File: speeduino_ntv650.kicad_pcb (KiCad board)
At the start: 2 copper layers, 105.1 x 96.7 mm, 70 parts, among them IC1 SP721, IC2 TC4424, J1 Conn_01x25_DB-25, P1 MAX9926_9927, Q1 STP62NS04Z, Q2 STP62NS04Z, Q3 STP62NS04Z, U1 LM2937xT

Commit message: first complited pcb
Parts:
- moved C13 52.2 mm to (108.2, 55.2)
- moved R9 37.3 mm to (91.2, 42.7), turned to 90 degrees
- moved C4 34.0 mm to (120.6, 55.2)
- moved C10 28.3 mm to (152.7, 81.3), turned to 0 degrees
- moved R18 26.0 mm to (108.8, 98.3), turned to 90 degrees
- moved C6 25.5 mm to (120.7, 40.9), turned to 270 degrees
- moved R14 23.8 mm to (105.8, 72.1)
- moved C8 23.4 mm to (132.2, 55.2), turned to 270 degrees
- moved C15 22.3 mm to (152.9, 89.1), turned to 0 degrees
- moved C16 20.9 mm to (126.7, 55.2), turned to 270 degrees
- moved R31 16.0 mm to (103.1, 98.4)
- moved R10 14.6 mm to (108.3, 45.9)
- moved R15 14.6 mm to (113.1, 45.9)
- moved R29 14.6 mm to (103.6, 45.9)
- moved R30 14.6 mm to (98.8, 45.9)
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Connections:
- C5 pad 1: MAP_5V -> 5V
- C6 pad 1: MAP_5V -> 5V
- J1 pad 16: MAP_5V -> 5V
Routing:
- net GND: track 485.5 -> 62.9 mm, vias 0 -> 12
- net 5V: track 240.8 -> 412.2 mm, vias 4 -> 2
- net MAP_5V: track 68.1 -> 0.00 mm, vias 2 -> 0
- net ADC-Clamp3: track 83.5 -> 138.1 mm
- net ADC-Clamp4: track 141.6 -> 93.0 mm
- net Net-(C2-Pad1): track 6.65 -> 49.4 mm
- net TACH2-CPU-D18: track 22.9 -> 60.9 mm, vias 0 -> 1
- net ADC-Clamp2: track 84.3 -> 121.2 mm, vias 2 -> 3
- net TPS_sens: track 176.4 -> 142.2 mm, vias 2 -> 1
- net Net-(C2-Pad2): track 5.64 -> 36.6 mm
- net ADC-Clamp1: track 103.5 -> 73.4 mm, vias 4 -> 1
- net ADC-Clamp6: track 102.3 -> 72.7 mm
- net Net-(C13-Pad1): track 103.4 -> 73.9 mm, vias 3 -> 0
- net IDLE-CPU-D6: track 70.5 -> 41.2 mm, vias 2 -> 0
- net MAP-CPU-A3: track 102.6 -> 74.2 mm, vias 1 -> 4
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- added copper zone on F.Cu, net (none)
- added copper zone on B.Cu, net GND
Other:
- board size 105.1 x 96.7 mm -> 105.2 x 102 mm
- net class 5v_small: clearance 0.11 -> 0.2; via_dia 0.8 -> 1.2; via_drill 0.4 -> 0.2
- net class Default: clearance 0.4 -> 0.2; via_dia 0.8 -> 1.2; via_drill 0.4 -> 0.2
- net class GND_MOSFIT: clearance 0.4 -> 0.3; via_dia 1 -> 1.2; via_drill 0.8 -> 0.2
- net class POWER_ENG: clearance 0.4 -> 0.28; via_dia 0.8 -> 1.2; via_drill 0.4 -> 0.2
- net class Power: clearance 0.4 -> 0.22; via_dia 1 -> 1.2; via_drill 0.6 -> 0.2
- net class power_exit: clearance 0.4 -> 0.3; via_dia 0.8 -> 1.2; via_drill 0.4 -> 0.2
- net class power_logic: via_dia 0.8 -> 1.2; via_drill 0.7 -> 0.2
- net class step_engine_exit: clearance 0.4 -> 0.3; via_dia 0.8 -> 1.2; via_drill 0.4 -> 0.2
- rule trace_clearance: 0.4 -> 0.2
- rule via_min_drill: 0.3 -> 0.2
- rule via_min_size: 0.4 -> 0.1

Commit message: new routes
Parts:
- C1, C11, C14, C2: moved to F.Cu
- moved R32 31.3 mm to (107.8, 107.7)
- moved R19 31.3 mm to (101.9, 107.9)
- moved R21 17.9 mm to (90.8, 89.0)
- moved R22 17.7 mm to (84.9, 89.0)
- moved R18 17.4 mm to (123.2, 108.2)
- moved R31 17.4 mm to (117.5, 108.2)
- moved C11 7.34 mm to (101.4, 62.5), turned to 90 degrees
- moved R1 3.45 mm to (137.2, 107.8)
- moved R2 3.45 mm to (131.8, 108.0)
- moved C18 3.11 mm to (74.5, 55.0)
- moved R25 0.72 mm to (121.7, 72.1)
- moved R23 0.31 mm to (114.7, 72.1)
- moved R24 0.31 mm to (135.1, 72.1)
- moved R26 0.31 mm to (128.3, 72.1)
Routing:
- net GND: track 62.9 -> 0.00 mm, vias 12 -> 0
- net 5V: track 412.2 -> 359.8 mm
- net MAP-CPU-A3: track 74.2 -> 122.7 mm, vias 4 -> 0
- net INJ2-CPU-D9: track 108.3 -> 67.8 mm, vias 1 -> 0
- net ADC-Clamp2: track 121.2 -> 85.6 mm, vias 3 -> 1
- net Net-(Q3-Pad1): track 18.3 -> 48.3 mm
- net ign-2-out: track 64.8 -> 93.8 mm, vias 1 -> 0
- net IDLE-CPU-D6: track 41.2 -> 13.3 mm
- net Net-(Q1-Pad1): track 8.40 -> 36.1 mm
- net Net-(C13-Pad1): track 73.9 -> 48.9 mm
- net INJ1-CPU-D8: track 50.1 -> 27.3 mm
- net ADC-Clamp3: track 138.1 -> 123.1 mm
- net Net-(Q2-Pad1): track 21.7 -> 7.96 mm
- net Net-(IC2-Pad7): track 21.9 -> 35.4 mm
- net ADC-Clamp4: track 93.0 -> 106.1 mm, vias 1 -> 2
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- added copper zone on F.Cu, net GND
- removed copper zone on F.Cu, net (none)

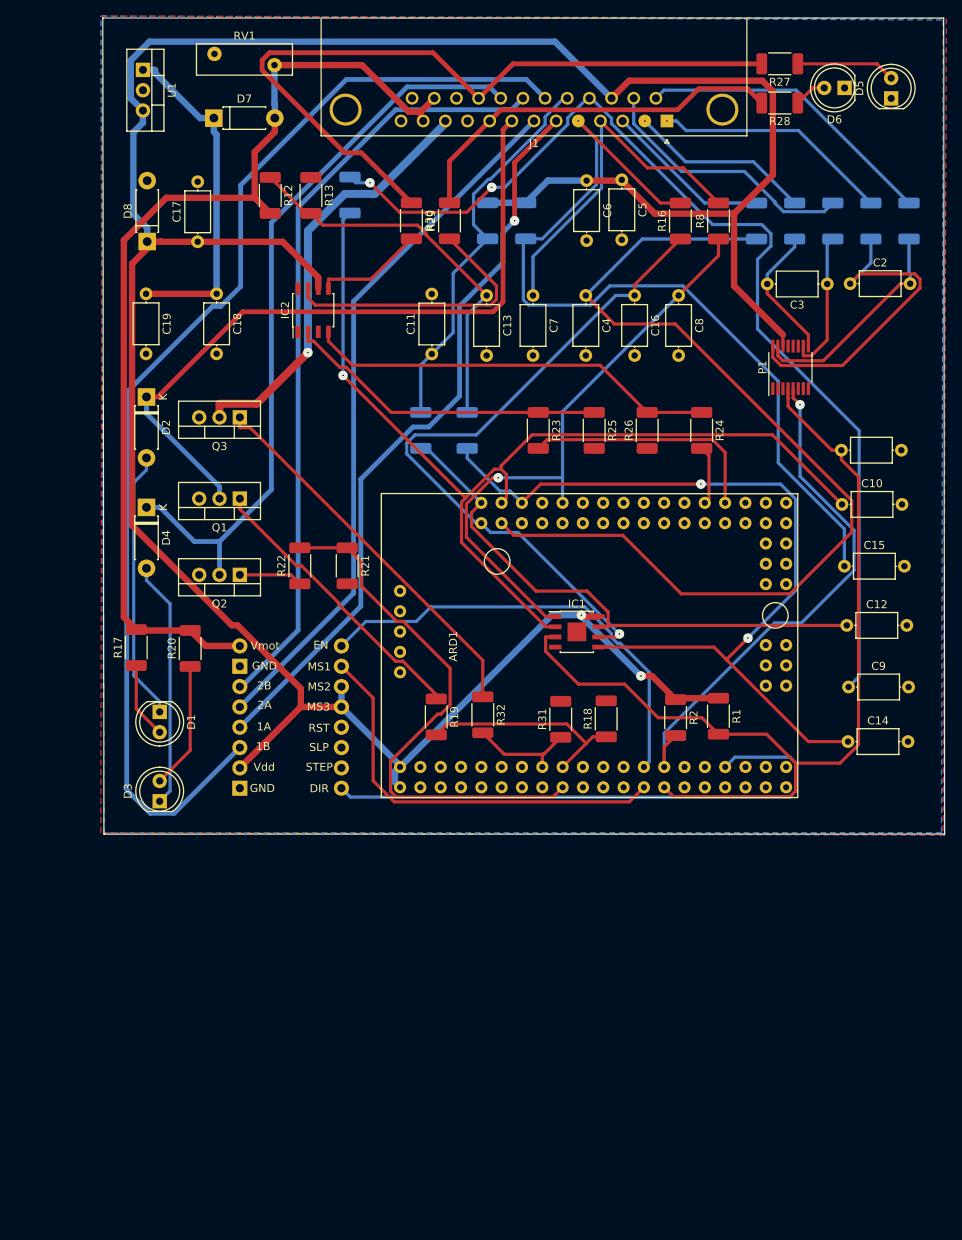
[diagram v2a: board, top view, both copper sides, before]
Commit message: pcb size chaged
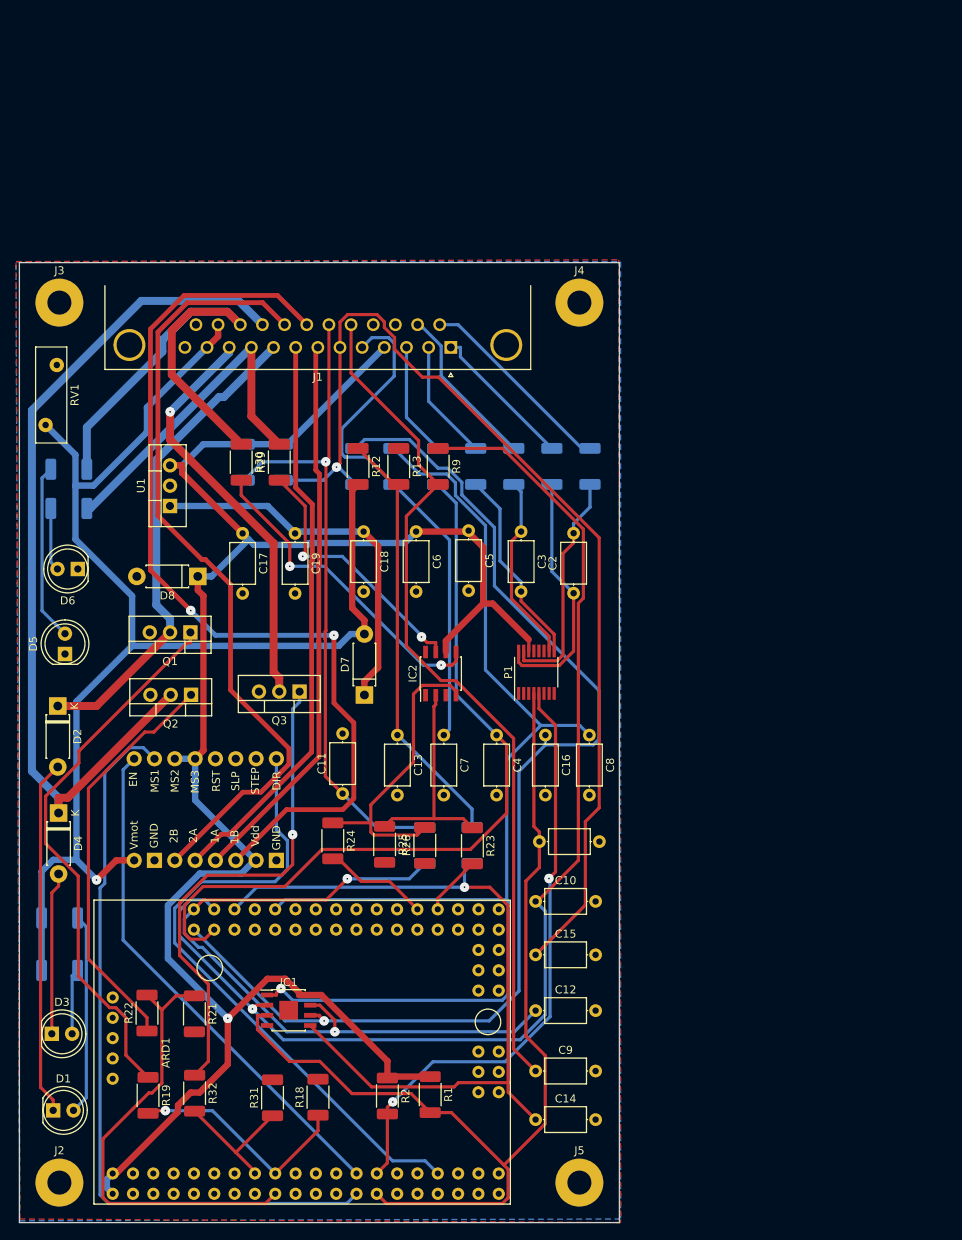
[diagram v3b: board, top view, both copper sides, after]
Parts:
- added J2: Conn_01x01, MountingHole:MountingHole_3mm_Pad, F.Cu at (54.8, 166.1)
- added J3: Conn_01x01, MountingHole:MountingHole_3mm_Pad, F.Cu at (54.8, 56.1)
- added J4: Conn_01x01, MountingHole:MountingHole_3mm_Pad, F.Cu at (119.8, 56.1)
- added J5: Conn_01x01, MountingHole:MountingHole_3mm_Pad, F.Cu at (119.8, 166.1)
- J1: value Conn_01x25_DB-25 -> DB25_Male_MountingHoles; footprint ntv650_ecu:DSUB-25_Male_Horizontal_P2.77x2.84mm_EdgePinOffset9.90mm_Housed_MountingHolesOffset11.32mm -> Connector_Dsub:DSUB-25_Male_Horizontal_P2.77x2.84mm_EdgePinOffset4.94mm_Housed_MountingHolesOffset7.48mm
- R16, R17, R20, R27, R28, R8: moved to B.Cu
- R9: moved to F.Cu
- moved D5 124.5 mm to (55.5, 100.0)
- moved D6 113.1 mm to (57.1, 89.4)
- moved R27 102.3 mm to (56.0, 77.0), turned to 0 degrees
- moved R28 102.3 mm to (56.0, 81.9), turned to 0 degrees
- moved D7 74.5 mm to (93.0, 105.2), turned to 90 degrees
- moved R24 69.0 mm to (89.0, 123.4)
- moved C10 62.7 mm to (114.3, 131.0)
- moved ARD1 62.2 mm to (64.0, 154.8)
- moved C15 62.0 mm to (114.3, 137.7)
- moved C9 61.9 mm to (114.3, 152.2)
- moved C12 61.9 mm to (114.3, 144.6)
- moved C1 61.8 mm to (122.3, 123.5)
- moved C14 61.3 mm to (114.3, 158.2)
- moved IC1 59.5 mm to (83.5, 144.6)
- moved R2 59.5 mm to (95.8, 155.3)
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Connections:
- J1 pad 0: (no net) -> GND
- J1 pad 10: (no net) -> ign-1-out
- J1 pad 16: 5V -> GND
- J1 pad 17: TPS_sens -> GND
- J1 pad 18: ITS_sens -> TPS_sens
- J1 pad 19: STEP-1B-OUT -> ITS_sens
- J1 pad 20: STEP-2B-OUT -> STEP-1B-OUT
- J1 pad 21: inj-2-out -> STEP-2B-OUT
- J1 pad 22: ign-2-out -> inj-2-out
- J1 pad 23: (no net) -> ign-2-out
- J1 pad 4: O2_sens -> 5V
- J1 pad 5: CLT_sens -> O2_sens
- J1 pad 6: STEP-1A-OUT -> CLT_sens
- J1 pad 7: STEP-2A-OUT -> STEP-1A-OUT
- J1 pad 8: inj-1-out -> STEP-2A-OUT
- J1 pad 9: ign-1-out -> inj-1-out
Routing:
- net 5V: track 359.8 -> 246.4 mm, vias 2 -> 1
- net ADC-Clamp1: track 73.8 -> 147.2 mm
- net ADC-Clamp2: track 85.6 -> 144.5 mm
- net Net-(Q2-Pad1): track 7.96 -> 51.0 mm
- net STEP-CPU-D17: track 51.6 -> 94.1 mm
- net 12V: track 126.4 -> 166.4 mm, vias 0 -> 1
- net ITS_sens: track 48.7 -> 82.9 mm, vias 0 -> 1
- net ign-2-out: track 93.8 -> 59.9 mm
- net Net-(Q1-Pad1): track 36.1 -> 69.1 mm
- net inj-1-out: track 89.2 -> 60.6 mm
- net Net-(IC2-Pad5): track 13.6 -> 40.5 mm, vias 0 -> 2
- net STEP-1B-OUT: track 145.3 -> 118.6 mm, vias 0 -> 2
- net ADC-Clamp3: track 123.1 -> 149.1 mm
- net MAP-CPU-A3: track 122.7 -> 97.7 mm
- net TPS_sens: track 131.4 -> 107.2 mm, vias 2 -> 0
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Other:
- board size 105.2 x 102 mm -> 75 x 120 mm
- net class GND_MOSFIT: trace_width 0.6 -> 1

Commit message: changed footprints
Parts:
- added C20: 47uF, Capacitors_SMD:CP_Elec_6.3x5.3, F.Cu at (64.2, 69.9)
- C18: footprint Capacitors_ThroughHole:C_Axial_L5.1mm_D3.1mm_P7.50mm_Horizontal -> Capacitors_SMD:CP_Elec_5x5.3
- C19: footprint Capacitors_ThroughHole:C_Axial_L5.1mm_D3.1mm_P7.50mm_Horizontal -> Capacitors_SMD:C_0805
- D7: footprint Diodes_ThroughHole:D_DO-41_SOD81_P7.62mm_Horizontal -> Diodes_ThroughHole:D_DO-41_SOD81_P5.08mm_Vertical_KathodeUp
- D8: footprint Diodes_ThroughHole:D_DO-41_SOD81_P7.62mm_Horizontal -> Diodes_ThroughHole:D_DO-201_P5.08mm_Vertical_KathodeUp
- RV1: footprint Varistors:RV_Disc_D12_W3.9_P7.5 -> Varistors:RV_Disc_D9_W3.3_P5
- moved U1 1.11 mm to (68.7, 80.4), turned to 180 degrees
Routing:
- net 5V: track 246.4 -> 0.00 mm, vias 1 -> 0
- net 12V: track 166.4 -> 0.00 mm, vias 1 -> 0
- net ADC-Clamp3: track 149.1 -> 0.00 mm, vias 1 -> 0
- net ADC-Clamp1: track 147.2 -> 0.00 mm, vias 1 -> 0
- net ADC-Clamp2: track 144.5 -> 0.00 mm, vias 1 -> 0
- net CLT_sens: track 130.1 -> 0.00 mm, vias 1 -> 0
- net ADC-Clamp5: track 125.4 -> 0.00 mm
- net STEP-1B-OUT: track 118.6 -> 0.00 mm, vias 2 -> 0
- net inj-2-out: track 108.7 -> 0.00 mm
- net TPS_sens: track 107.2 -> 0.00 mm
- net STEP-2B-OUT: track 98.8 -> 0.00 mm
- net MAP-CPU-A3: track 97.7 -> 0.00 mm
- net ADC-Clamp4: track 96.0 -> 0.00 mm, vias 1 -> 0
- net STEP-CPU-D17: track 94.1 -> 0.00 mm
- net ADC-Clamp6: track 90.1 -> 0.00 mm, vias 2 -> 0
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
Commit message: routing
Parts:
- added C21: 1nF, Capacitors_SMD:C_0805_HandSoldering, F.Cu at (109.7, 77.9)
- A1: moved to F.Cu
- C1, C10, C11, C12, C13, C14, C15, C16, C17, C3, C4, C5, C6, C7, C8, C9: footprint Capacitors_ThroughHole:C_Axial_L5.1mm_D3.1mm_P7.50mm_Horizontal -> Capacitors_SMD:C_0805_HandSoldering
- C19: footprint Capacitors_SMD:C_0805 -> Capacitors_SMD:C_0805_HandSoldering
- C2: value 1nF -> 0.22mF; footprint Capacitors_ThroughHole:C_Axial_L5.1mm_D3.1mm_P7.50mm_Horizontal -> Capacitors_SMD:C_0805_HandSoldering
- D1, D3, D5, D6: footprint LED_THT:LED_D5.0mm -> LEDs:LED_0805_HandSoldering
- D2, D4: footprint Diode_THT:D_DO-41_SOD81_P7.62mm_Horizontal -> Diodes_ThroughHole:D_A-405_P2.54mm_Vertical_AnodeUp
- R1, R12, R13, R18, R19, R2, R21, R22, R23, R24, R25, R26, R31, R32, R9: footprint Resistor_SMD:R_2010_5025Metric -> Resistors_SMD:R_0805_HandSoldering
- R10, R11, R14, R15, R16, R17, R20, R27, R28, R3, R4, R5, R6, R7, R8: footprint Resistor_SMD:R_2010_5025Metric -> Resistors_SMD:R_0805_HandSoldering; moved to F.Cu
- R29, R30: footprint Resistor_SMD:R_2010_5025Metric -> Resistors_ThroughHole:R_Axial_DIN0207_L6.3mm_D2.5mm_P2.54mm_Vertical
- RV1: footprint Varistors:RV_Disc_D9_W3.3_P5 -> Varistors:RV_Disc_D15.5_W3.9_P7.5
- moved RV1 101.5 mm to (103.7, 159.4), turned to 0 degrees
- moved C20 95.8 mm to (66.7, 165.7)
- moved U1 88.8 mm to (88.0, 167.1), turned to 0 degrees
- moved R10 87.8 mm to (120.5, 152.9)
- moved D8 85.4 mm to (110.7, 166.6)
- moved C18 81.8 mm to (77.6, 165.1), turned to 0 degrees
- moved R1 68.6 mm to (122.5, 89.9)
- moved R12 67.4 mm to (53.7, 132.0)
- moved R13 65.1 mm to (53.9, 125.1)
- moved R16 62.8 mm to (88.7, 139.3), turned to 180 degrees
- moved C11 61.2 mm to (120.7, 64.4)
- moved C5 56.6 mm to (95.0, 140.2), turned to 180 degrees
- moved D7 54.7 mm to (88.0, 159.6), turned to 0 degrees
- moved D2 53.8 mm to (61.6, 159.9), turned to 180 degrees
- moved C15 52.7 mm to (102.6, 86.3), turned to 90 degrees
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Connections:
- C2 pad 1: Net-(C2-Pad1) -> GND
- C2 pad 2: Net-(C2-Pad2) -> (no net)
- P1 pad 10: Net-(C3-Pad1) -> Net-(C21-Pad1)
- P1 pad 15: Net-(C2-Pad2) -> Net-(C3-Pad2)
- P1 pad 16: Net-(C2-Pad1) -> Net-(C3-Pad1)
- P1 pad 9: Net-(C3-Pad2) -> Net-(C21-Pad2)
- R3 pad 2: Net-(C2-Pad1) -> Net-(C3-Pad1)
- R4 pad 2: Net-(C2-Pad2) -> Net-(C3-Pad2)
- R5 pad 2: Net-(C3-Pad1) -> Net-(C21-Pad1)
- R6 pad 2: Net-(C3-Pad2) -> Net-(C21-Pad2)

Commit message: -
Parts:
- moved D8 110.2 mm to (61.3, 68.0), turned to 270 degrees
- moved RV1 97.9 mm to (54.2, 75.0), turned to 90 degrees
- moved Q2 89.3 mm to (90.2, 165.3), turned to 90 degrees
- moved Q3 88.8 mm to (81.9, 160.9), turned to 270 degrees
- moved U1 80.8 mm to (61.9, 90.7), turned to 90 degrees
- moved Q1 78.4 mm to (101.3, 160.8), turned to 270 degrees
- moved D7 76.7 mm to (54.4, 90.7), turned to 90 degrees
- moved R14 71.1 mm to (71.6, 167.2)
- moved C18 66.5 mm to (59.9, 101.1), turned to 90 degrees
- moved R19 57.9 mm to (111.5, 158.3), turned to 90 degrees
- moved C20 54.0 mm to (60.4, 112.0), turned to 90 degrees
- moved C19 42.9 mm to (60.7, 160.1), turned to 0 degrees
- moved C13 39.4 mm to (55.1, 157.1)
- moved D5 39.4 mm to (59.8, 149.1)
- moved D6 39.4 mm to (54.9, 149.7)
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
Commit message: -
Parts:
- IC2: footprint Housings_SOIC:SOIC-8_3.9x4.9mm_Pitch1.27mm -> Housings_DIP:DIP-8_W7.62mm
- moved Q1 71.5 mm to (56.2, 105.2), turned to 0 degrees
- moved R13 67.0 mm to (120.7, 122.8)
- moved R12 66.2 mm to (120.3, 115.7)
- moved C13 65.6 mm to (120.3, 150.8)
- moved C19 64.5 mm to (67.9, 96.0), turned to 90 degrees
- moved Q2 58.9 mm to (59.3, 115.1), turned to 180 degrees
- moved Q3 46.3 mm to (54.9, 123.3), turned to 0 degrees
- moved R14 42.3 mm to (112.9, 158.0)
- moved C16 28.4 mm to (96.4, 134.2)
- moved C10 26.9 mm to (96.3, 139.4)
- moved R8 24.3 mm to (96.2, 144.1)
- moved R18 23.6 mm to (96.2, 149.1), turned to 180 degrees
- moved IC1 21.4 mm to (88.1, 150.2)
- moved C17 21.0 mm to (111.0, 101.4), turned to 90 degrees
- moved R32 20.9 mm to (80.0, 136.3)
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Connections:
- R29 pad 1: Net-(IC2-Pad7) -> ign-1-out
- R29 pad 2: ign-1-out -> Net-(IC2-Pad7)

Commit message: fixed errors
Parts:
- D2, D4: footprint Diodes_ThroughHole:D_A-405_P2.54mm_Vertical_AnodeUp -> Diodes_SMD:D_SOD-323_HandSoldering
- moved R10 82.9 mm to (95.5, 70.9)
- moved C12 62.8 mm to (118.0, 101.6), turned to 90 degrees
- moved R11 62.3 mm to (120.5, 109.3), turned to 90 degrees
- moved C2 37.6 mm to (80.0, 148.2), turned to 0 degrees
- moved R14 28.5 mm to (113.0, 129.6), turned to 90 degrees
- moved IC1 27.5 mm to (90.0, 122.8), turned to 180 degrees
- moved R16 22.7 mm to (97.4, 129.7)
- moved R19 18.5 mm to (97.4, 154.8), turned to 0 degrees
- moved R32 16.2 mm to (80.0, 152.5)
- moved R25 15.4 mm to (101.4, 108.7)
- moved R23 13.7 mm to (113.8, 151.0)
- moved C13 13.5 mm to (120.3, 137.2)
- moved R1 12.3 mm to (106.8, 101.4)
- moved C1 11.5 mm to (95.9, 108.7)
- moved C17 8.98 mm to (102.0, 101.7)
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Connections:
- C2 pad 2: (no net) -> TACH2-CPU-D18
- J1 pad 4: 5V -> (no net)
